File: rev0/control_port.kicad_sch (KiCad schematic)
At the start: 26 parts, among them IC1 ECP5-BGA256, U16 PI3USB102G, U8 USB3343-CP

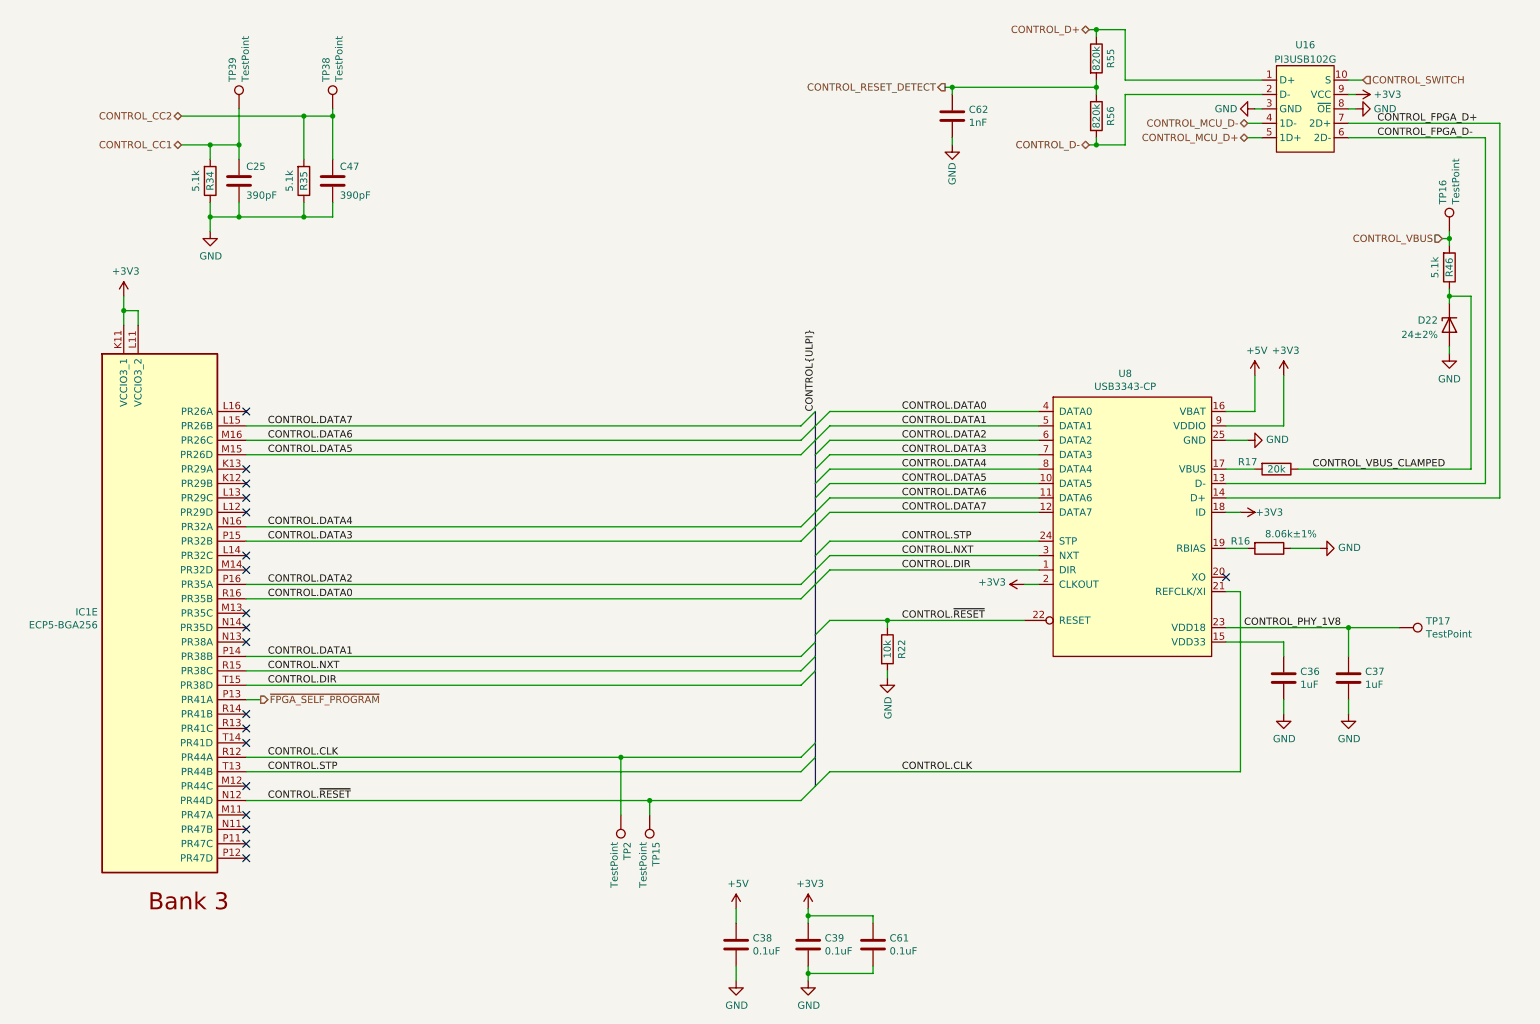
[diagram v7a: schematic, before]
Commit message: hardware: update layout to match schematic
- invert USB switch D+/D- for routing convenience
- connect *_VBUS_CLAMPED to *_VBUS_IN not *_VBUS
- reassign FPGA pins and banks for routing convenience
- connect PHY VBAT to +3V3, not +5V
- add PHY VDD33 test points
- add LED test points
- add PROGRAM button test point
- add PHY VDD33 test point
- add mezzanine connector
- improve decoupling
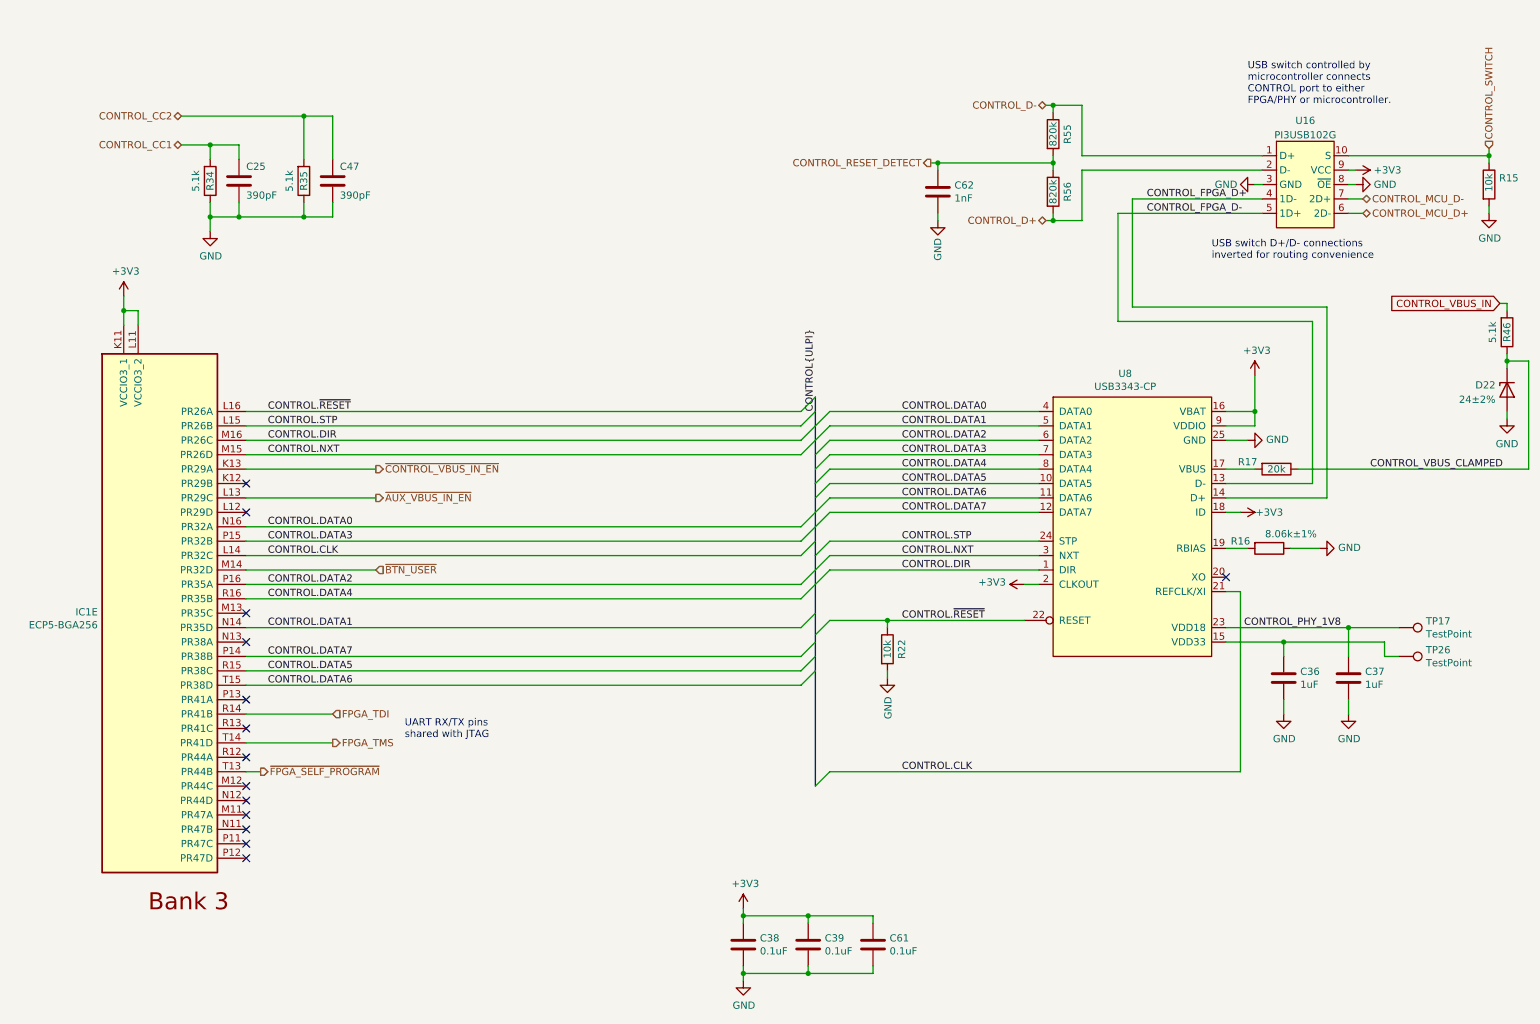
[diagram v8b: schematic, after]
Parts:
- removed TP15, TP16, TP2, TP38, TP39: TestPoint, TestPoint:TestPoint_Pad_D1.0mm, symbol Connector:TestPoint
- added R15: 10k, Resistor_SMD:R_0402_1005Metric, symbol Device:R
- added TP26: TestPoint, TestPoint:TestPoint_Pad_D1.0mm, symbol Connector:TestPoint
- C36, C37: footprint Capacitor_SMD:C_0603_1608Metric -> Capacitor_SMD:C_0402_1005Metric; Manufacturer (none) -> Samsung; Part Number GENERIC-CAP-0603-1uF -> CL05A105MQ5NNNC; Substitution any equivalent -> (none)
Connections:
- net +5V is gone; now on net +3V3: C38.1, U8.16 (VBAT)
- net CONTROL.CLK: now also IC1.L14 (PR32C); no longer IC1.R12 (PR44A)
- net CONTROL.DATA0: now also IC1.N16 (PR32A); no longer IC1.R16 (PR35B)
- net CONTROL.DATA1: now also IC1.N14 (PR35D); no longer IC1.P14 (PR38B)
- net CONTROL.DATA4: now also IC1.R16 (PR35B); no longer IC1.N16 (PR32A)
- net CONTROL.DATA5: now also IC1.R15 (PR38C); no longer IC1.M15 (PR26D)
- net CONTROL.DATA6: now also IC1.T15 (PR38D); no longer IC1.M16 (PR26C)
- net CONTROL.DATA7: now also IC1.P14 (PR38B); no longer IC1.L15 (PR26B)
- net CONTROL.DIR: now also IC1.M16 (PR26C); no longer IC1.T15 (PR38D)
- net CONTROL.NXT: now also IC1.M15 (PR26D); no longer IC1.R15 (PR38C)
- net CONTROL.STP: now also IC1.L15 (PR26B); no longer IC1.T13 (PR44B)
- net CONTROL.~{RESET}: now also IC1.L16 (PR26A); no longer IC1.N12 (PR44D)
- net CONTROL_D+: now also R56.2, U16.2 (D-); no longer R55.1, U16.1 (D+)
- net CONTROL_D-: now also R55.1, U16.1 (D+); no longer R56.2, U16.2 (D-)
- net CONTROL_FPGA_D+: now also U16.4 (1D-); no longer U16.7 (2D+)
- net CONTROL_FPGA_D-: now also U16.5 (1D+); no longer U16.6 (2D-)
- net CONTROL_MCU_D+: now also U16.6 (2D-); no longer U16.5 (1D+)
- net CONTROL_MCU_D-: now also U16.7 (2D+); no longer U16.4 (1D-)
- net CONTROL_SWITCH: now also R15.1
- net GND: now also R15.2
- net ~{FPGA_SELF_PROGRAM}: now also IC1.T13 (PR44B); no longer IC1.P13 (PR41A)
- net at C36.1, U8.15 (VDD33): now also TP26.1
- net ~{CONTROL_VBUS_IN_EN}: now reaches IC1.K13 (PR29A)
- net ~{AUX_VBUS_IN_EN}: now reaches IC1.L13 (PR29C)
- net ~{BTN_USER}: now reaches IC1.M14 (PR32D)
- net FPGA_TDI: now reaches IC1.R14 (PR41B)
- net FPGA_TMS: now reaches IC1.T14 (PR41D)
- net CONTROL_VBUS renamed CONTROL_VBUS_IN
- no-connect marks 19 -> 14
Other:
- note added: "UART RX/TX pins shared with JTAG"
- note added: "USB switch D+/D- connections inverted for routing convenience"
- note added: "USB switch controlled by microcontroller connects CONTROL port to either FPGA/PHY or microcontroller."
- moved on the sheet: C38, C62, D22, R46, R55, R56, U16
